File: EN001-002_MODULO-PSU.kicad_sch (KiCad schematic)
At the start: 90 parts, among them J1 2x5P 2.54mm, J2 Conn_01x02, J3 Barrel_Jack_Switch, J5 1x3P 2mm, J6 Conn_01x04, Q10 AO3401, Q11 KY6802, Q13 MMBT2222A, Q2 AO3401, Q3 KY6802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

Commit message: pcb layout
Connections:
- net GND: now also SW1.1 (A); no longer SW1.3 (C)
- net at R36.1: now also SW1.3 (C); no longer SW1.1 (A)
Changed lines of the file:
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@@
 		(lib_id "00_EV_DATABASE:SWITCH/SW_Slide_SPDT_Angled")
 		(at 31.75 147.32 0)
+		(mirror x)
 		(unit 1)
 		(exclude_from_sim no)
@@
 		(on_board yes)
 		(dnp no)
-		(fields_autoplaced yes)
 		(property "Reference" "SW1"
-			(at 31.75 138.43 0)
+			(at 31.75 156.21 0)
 			(effects
 				(font
@@
 		)
 		(property "Value" "SK12D07VG3"
-			(at 31.75 140.97 0)
+			(at 31.75 153.67 0)
 			(effects
 				(font
@@
 		)
 		(property "Datasheet" "~"
-			(at 31.75 154.94 0)
+			(at 31.75 139.7 0)
 			(effects
 				(font

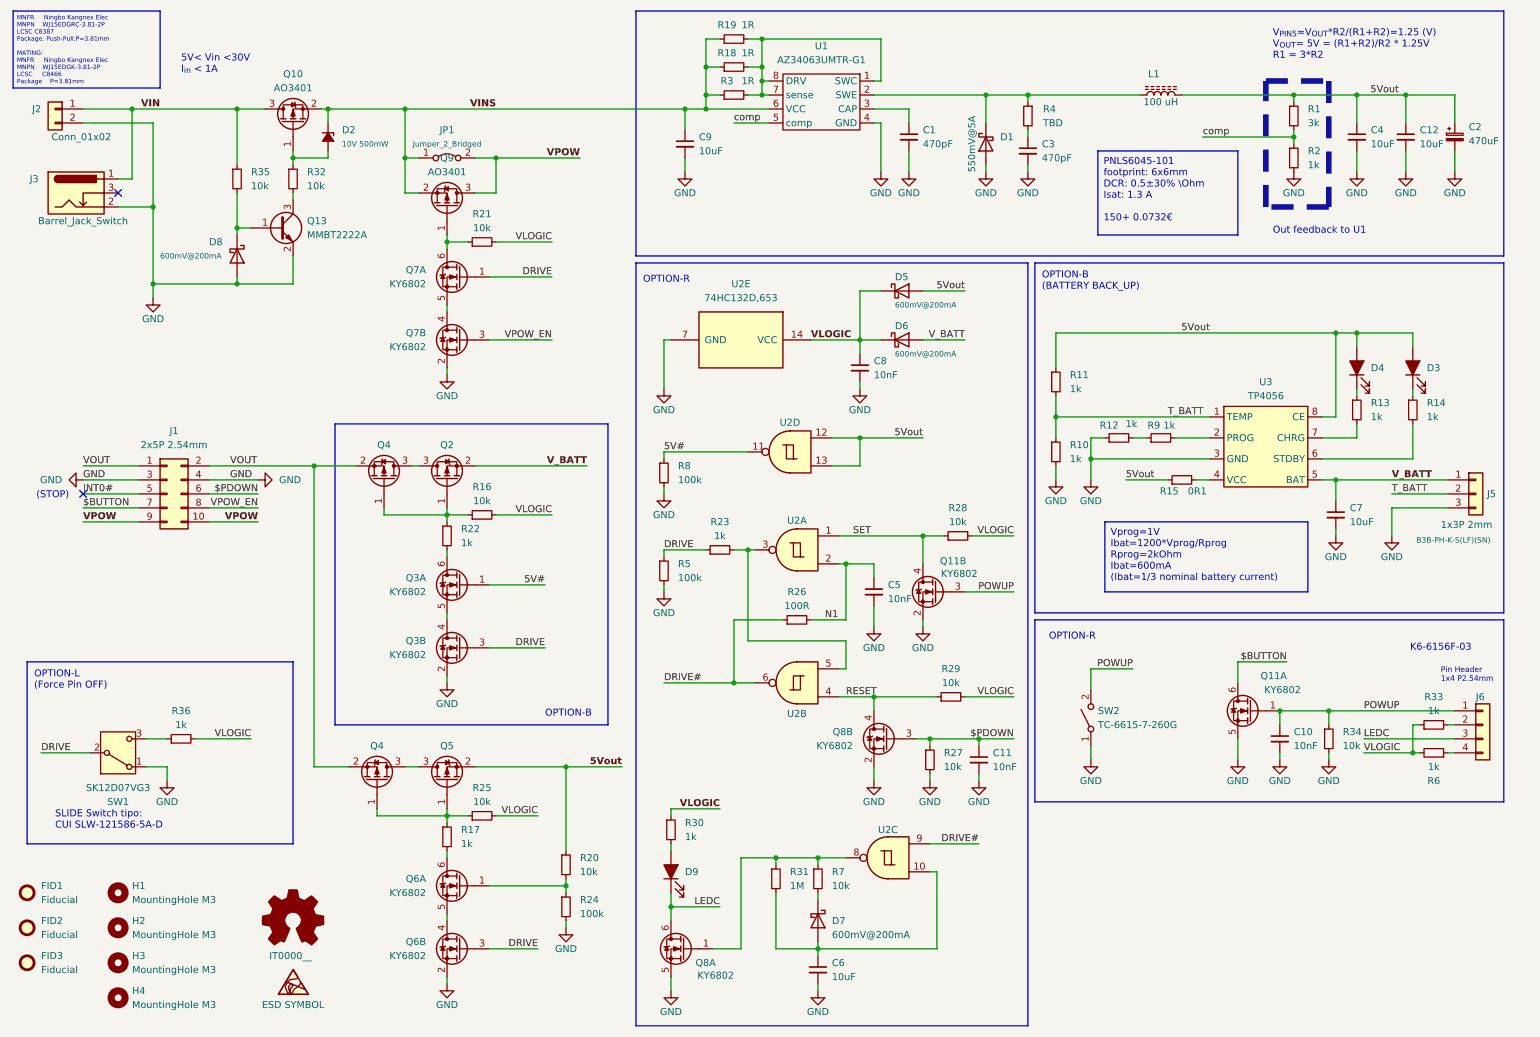
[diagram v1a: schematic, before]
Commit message: Rotated D7, SW2 in parallel to external switch, removed R26 replaced with short, removed C5
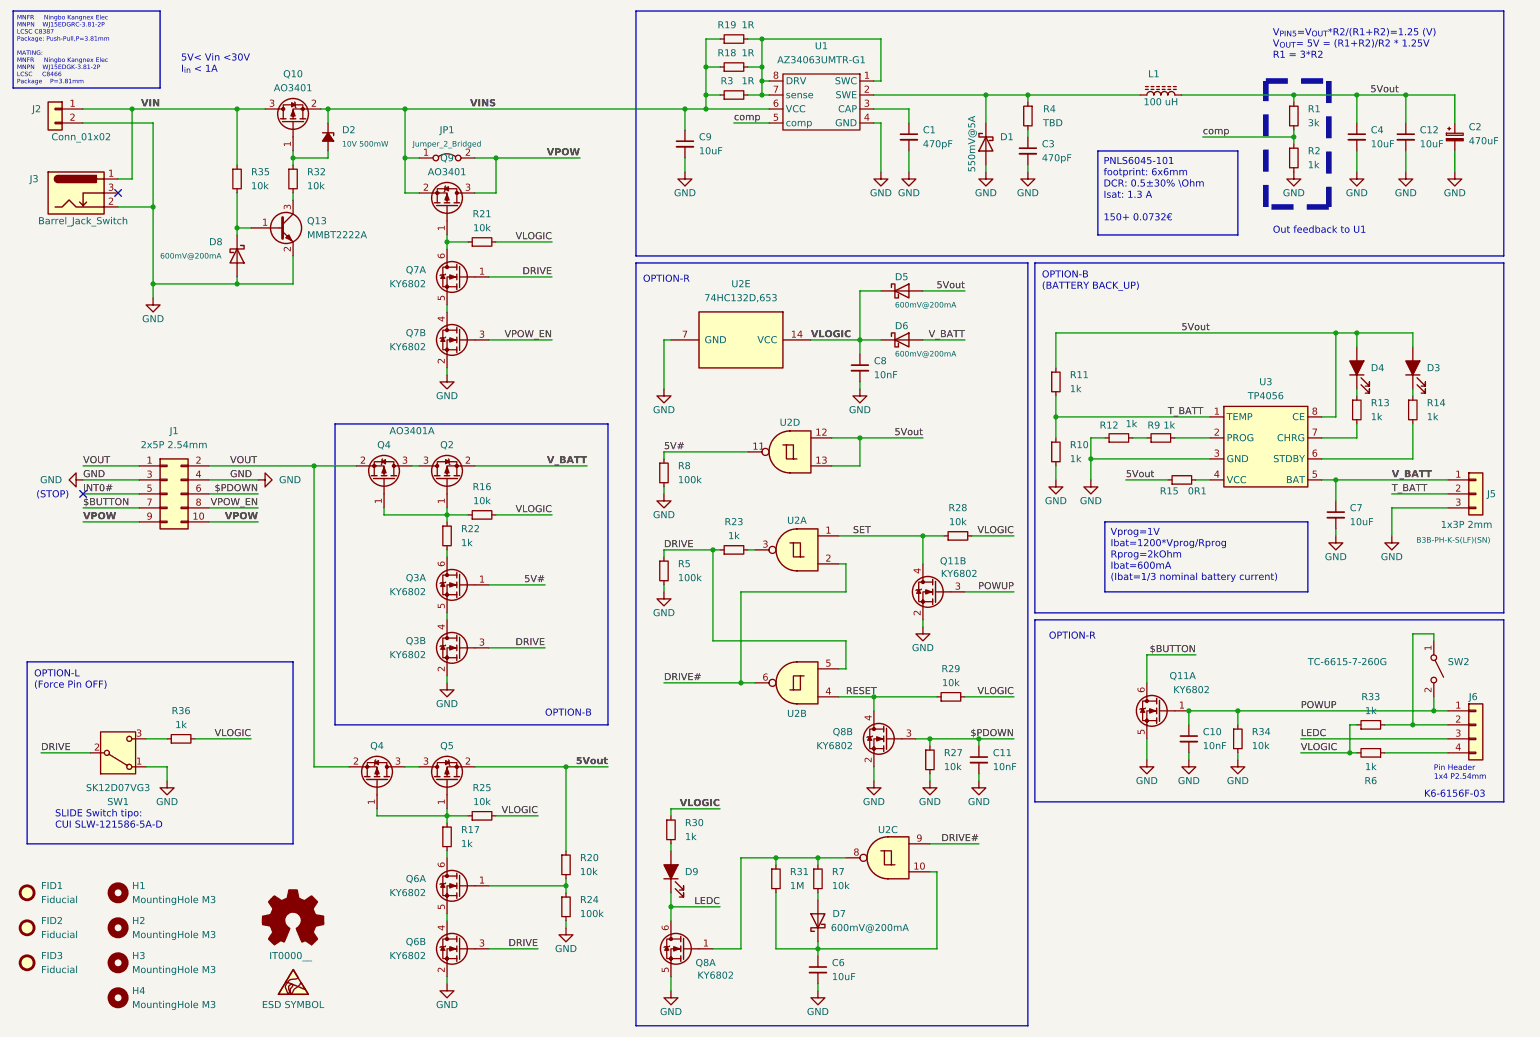
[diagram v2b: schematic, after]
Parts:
- removed C5: 10nF, Capacitor_SMD:C_0805_2012Metric_Pad1.18x1.45mm_HandSolder, symbol 00_EV_DATABASE:MLCC/CC0805KRX7R9BB103
- removed R26: 100R, Resistor_SMD:R_0805_2012Metric_Pad1.20x1.40mm_HandSolder, symbol 00_EV_DATABASE:Res-SMD/0805_100R
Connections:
- net N1 is gone; now on net DRIVE#: U2.2
- net DRIVE: now also U2.5
- net GND: no longer SW2.1 (A)
- net at J6.2 (Pin_2), R33.2: now also SW2.1 (A)
- net at R23.2, U2.3: no longer U2.5
- net at R7.2: now also D7.2 (A); no longer D7.1 (K)
- net at C6.1, R31.2, U2.10: now also D7.1 (K); no longer D7.2 (A)
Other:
- moved on the sheet: C10, D7, J6, Q11A, R23, R33, R34, R6, SW2

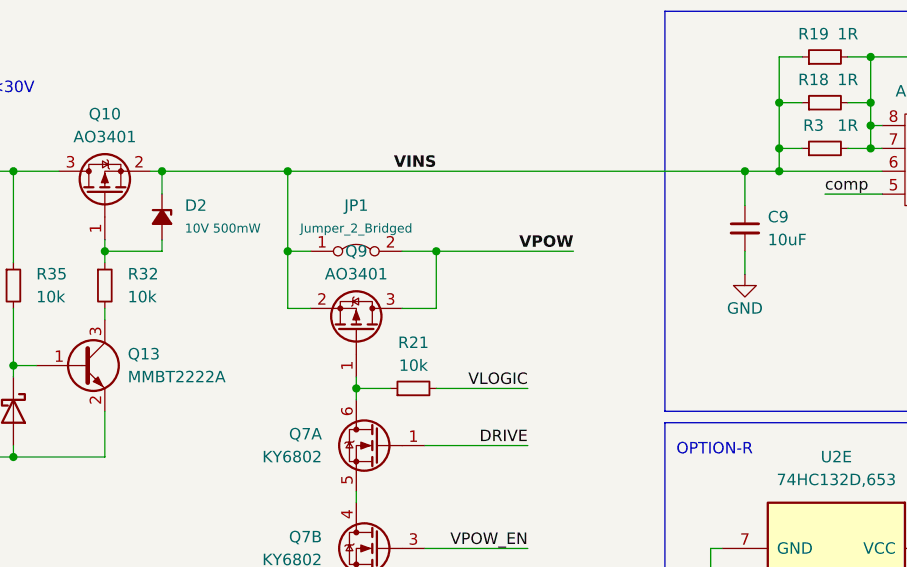
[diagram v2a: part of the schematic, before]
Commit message: R21 moved betwwen source and drain of Q9
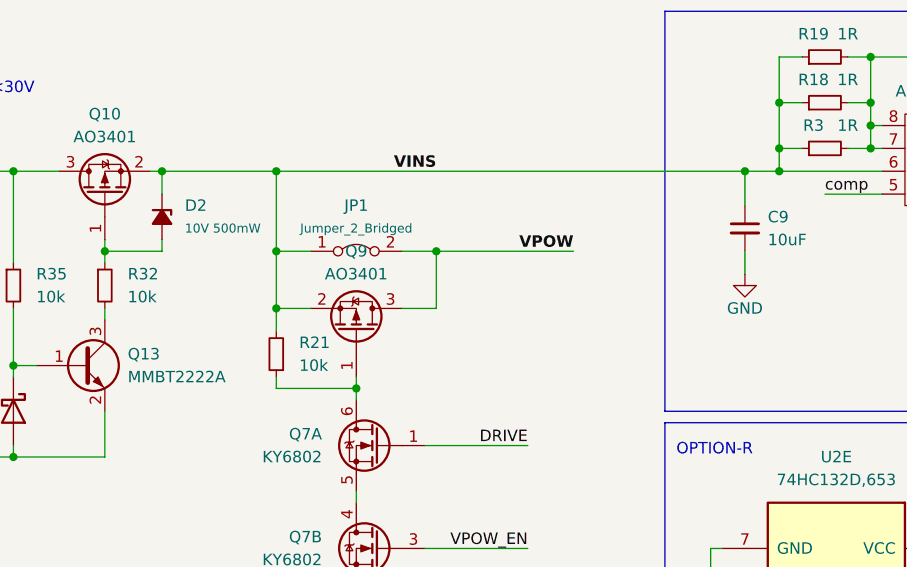
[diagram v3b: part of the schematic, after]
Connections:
- net VINS: now also R21.2
- net VLOGIC: no longer R21.2
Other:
- moved on the sheet: R21
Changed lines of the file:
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@@
 	)
 	(junction
+		(at 91.44 54.61)
+		(diameter 0)
+		(color 0 0 0 0)
+	)
+	(junction
 		(at 252.73 97.79)
 		(diameter 0)
@@
 	)
 	(junction
-		(at 113.03 149.86)
+		(at 82.55 30.48)
 		(diameter 0)
 		(color 0 0 0 0)
 	)
 	(junction
-		(at 91.44 54.61)
+		(at 113.03 149.86)
 		(diameter 0)
 		(color 0 0 0 0)
@@
 	)
 	(junction
-		(at 83.82 39.37)
-		(diameter 0)
-		(color 0 0 0 0)
-	)
-	(junction
 		(at 139.7 110.49)
 		(diameter 0)
@@
 	)
 	(junction
+		(at 82.55 45.72)
+		(diameter 0)
+		(color 0 0 0 0)
+	)
+	(junction
 		(at 166.37 90.17)
 		(diameter 0)
@@
 	)
 	(junction
+		(at 82.55 39.37)
+		(diameter 0)
+		(color 0 0 0 0)
+	)
+	(junction
 		(at 208.28 93.98)
 		(diameter 0)
@@
 	)
 	(junction
-		(at 83.82 30.48)
-		(diameter 0)
-		(color 0 0 0 0)
-	)
-	(junction
 		(at 113.03 171.45)
 		(diameter 0)
@@
 	(wire
 		(pts
-			(xy 91.44 55.88) (xy 91.44 54.61)
-		)
-		(stroke
-			(width 0)
-			(type default)
-		)
-	)
-	(wire
-		(pts
 			(xy 227.33 129.54) (xy 218.44 129.54)
 		)
@@
 	(wire
 		(pts
-			(xy 86.36 45.72) (xy 83.82 45.72)
-		)
-		(stroke
-			(width 0)
-			(type default)
-		)
-	)
-	(wire
-		(pts
 			(xy 189.23 27.94) (xy 168.91 27.94)
 		)
@@
 	(wire
 		(pts
-			(xy 83.82 30.48) (xy 83.82 39.37)
+			(xy 82.55 30.48) (xy 82.55 39.37)
 		)
 		(stroke
@@
 	(wire
 		(pts
+			(xy 82.55 54.61) (xy 91.44 54.61)
+		)
+		(stroke
+			(width 0)
+			(type default)
+		)
+	)
+	(wire
+		(pts
 			(xy 262.89 102.87) (xy 262.89 107.95)
 		)
@@
 	(wire
 		(pts
+			(xy 82.55 53.34) (xy 82.55 54.61)
+		)
+		(stroke
+			(width 0)
+			(type default)
+		)
+	)
+	(wire
+		(pts
 			(xy 163.83 113.03) (xy 163.83 118.11)
 		)
@@
 	(wire
 		(pts
-			(xy 162.56 132.08) (xy 163.83 132.08)
+			(xy 82.55 30.48) (xy 134.62 30.48)
 		)
 		(stroke
@@
 	(wire
 		(pts
-			(xy 132.08 157.48) (xy 132.08 158.75)
+			(xy 162.56 132.08) (xy 163.83 132.08)
 		)
 		(stroke
@@
 	(wire
 		(pts
-			(xy 100.33 54.61) (xy 110.49 54.61)
+			(xy 132.08 157.48) (xy 132.08 158.75)
 		)
 		(stroke
@@
 	(wire
 		(pts
-			(xy 83.82 39.37) (xy 86.36 39.37)
-		)
-		(stroke
-			(width 0)
-			(type default)
-		)
-	)
-	(wire
-		(pts
 			(xy 185.42 137.16) (xy 194.31 137.16)
 		)
@@
 	(wire
 		(pts
+			(xy 82.55 39.37) (xy 86.36 39.37)
+		)
+		(stroke
+			(width 0)
+			(type default)
+		)
+	)
+	(wire
+		(pts
 			(xy 256.54 27.94) (xy 265.43 27.94)
 		)
@@
 	(wire
 		(pts
+			(xy 82.55 48.26) (xy 82.55 45.72)
+		)
+		(stroke
+			(width 0)
+			(type default)
+		)
+	)
+	(wire
+		(pts
 			(xy 201.93 97.79) (xy 201.93 95.25)
 		)
@@
 	(wire
 		(pts
-			(xy 69.85 30.48) (xy 83.82 30.48)
+			(xy 69.85 30.48) (xy 82.55 30.48)
 		)
 		(stroke
@@
 	(wire
 		(pts
-			(xy 91.44 54.61) (xy 95.25 54.61)
+			(xy 40.64 149.86) (xy 36.83 149.86)
 		)
 		(stroke
@@
 	(wire
 		(pts
-			(xy 40.64 149.86) (xy 36.83 149.86)
+			(xy 270.51 125.73) (xy 266.7 125.73)
 		)
 		(stroke
@@
 	(wire
 		(pts
-			(xy 270.51 125.73) (xy 266.7 125.73)
+			(xy 91.44 53.34) (xy 91.44 54.61)
 		)
 		(stroke
@@
 	(wire
 		(pts
-			(xy 91.44 54.61) (xy 91.44 53.34)
+			(xy 218.44 129.54) (xy 218.44 134.62)
 		)
 		(stroke
@@
 	(wire
 		(pts
-			(xy 218.44 129.54) (xy 218.44 134.62)
+			(xy 166.37 63.5) (xy 166.37 72.39)
 		)
 		(stroke
@@
 	(wire
 		(pts
-			(xy 166.37 63.5) (xy 166.37 72.39)
+			(xy 158.75 173.99) (xy 158.75 172.72)
 		)
 		(stroke
@@
 	(wire
 		(pts
-			(xy 158.75 173.99) (xy 158.75 172.72)
+			(xy 82.55 45.72) (xy 86.36 45.72)
 		)
 		(stroke
@@
 	(wire
 		(pts
-			(xy 83.82 45.72) (xy 83.82 39.37)
+			(xy 82.55 45.72) (xy 82.55 39.37)
 		)
 		(stroke
@@
 	(wire
 		(pts
-			(xy 261.62 142.24) (xy 266.7 142.24)
+			(xy 91.44 54.61) (xy 91.44 55.88)
 		)
 		(stroke
@@
 	(wire
 		(pts
-			(xy 63.5 57.15) (xy 63.5 62.23)
+			(xy 261.62 142.24) (xy 266.7 142.24)
 		)
 		(stroke
@@
 	(wire
 		(pts
-			(xy 83.82 30.48) (xy 134.62 30.48)
+			(xy 63.5 57.15) (xy 63.5 62.23)
 		)
 		(stroke
@@
 	)
 	(label "VLOGIC"
-		(at 110.49 54.61 180)
-		(fields_autoplaced yes)
-		(effects
-			(font
-				(size 1.27 1.27)
-			)
-			(justify right bottom)
-		)
-	)
-	(label "VLOGIC"
 		(at 55.88 144.78 180)
 		(fields_autoplaced yes)
@@
 	(symbol
 		(lib_id "00_EV_DATABASE:Res-SMD/0805_10k")
-		(at 97.79 54.61 90)
+		(at 82.55 50.8 180)
 		(unit 1)
 		(exclude_from_sim no)
@@
 		(fields_autoplaced yes)
 		(property "Reference" "R21"
-			(at 97.79 49.53 90)
+			(at 85.09 49.5299 0)
 			(effects
 				(font
 					(size 1.27 1.27)
 				)
+				(justify right)
 			)
 		)
 		(property "Value" "10k"
-			(at 97.79 52.07 90)
+			(at 85.09 52.0699 0)
 			(effects
 				(font
 					(size 1.27 1.27)
 				)
+				(justify right)
 			)
 		)
 		(property "Footprint" "Resistor_SMD:R_0805_2012Metric_Pad1.20x1.40mm_HandSolder"
-			(at 97.79 54.61 0)
+			(at 82.55 50.8 0)
 			(effects
 				(font
@@
 		)
 		(property "Datasheet" "~"
-			(at 97.79 54.61 0)
+			(at 82.55 50.8 0)
 			(effects
 				(font
@@
 		)
 		(property "Description" "Thin Film Resistor 10kΩ 125mW 150V ±1% ±100ppm/℃ "
-			(at 97.79 54.61 0)
+			(at 82.55 50.8 0)
 			(effects
 				(font
@@
 		)
 		(property "MNFR-1" "UNI-ROYAL"
-			(at 97.79 54.61 0)
+			(at 82.55 50.8 0)
 			(show_name yes)
 			(effects
@@
 		)
 		(property "MNFR-1-PN" "0805W8F1002T5E"
-			(at 97.79 54.61 0)
+			(at 82.55 50.8 0)
 			(show_name yes)
 			(effects
@@
 		)
 		(property "SUPP-1" "LCSC"
-			(at 97.79 54.61 0)
+			(at 82.55 50.8 0)
 			(show_name yes)
 			(effects
@@
 		)
 		(property "SUPP-1-CODE" "C17414"
-			(at 97.79 54.61 0)
+			(at 82.55 50.8 0)
 			(show_name yes)
 			(effects
@@
 		)
 		(property "Case" "0805"
-			(at 97.79 54.61 0)
+			(at 82.55 50.8 0)
 			(show_name yes)
 			(effects
@@
 		)
 		(property "STOCK" "1000"
-			(at 97.79 54.61 0)
+			(at 82.55 50.8 0)
 			(show_name yes)
 			(effects
@@
 		)
 		(property "SUPP-1-UNIT-PRICE" "0.0013"
-			(at 97.79 54.61 0)
+			(at 82.55 50.8 0)
 			(effects
 				(font

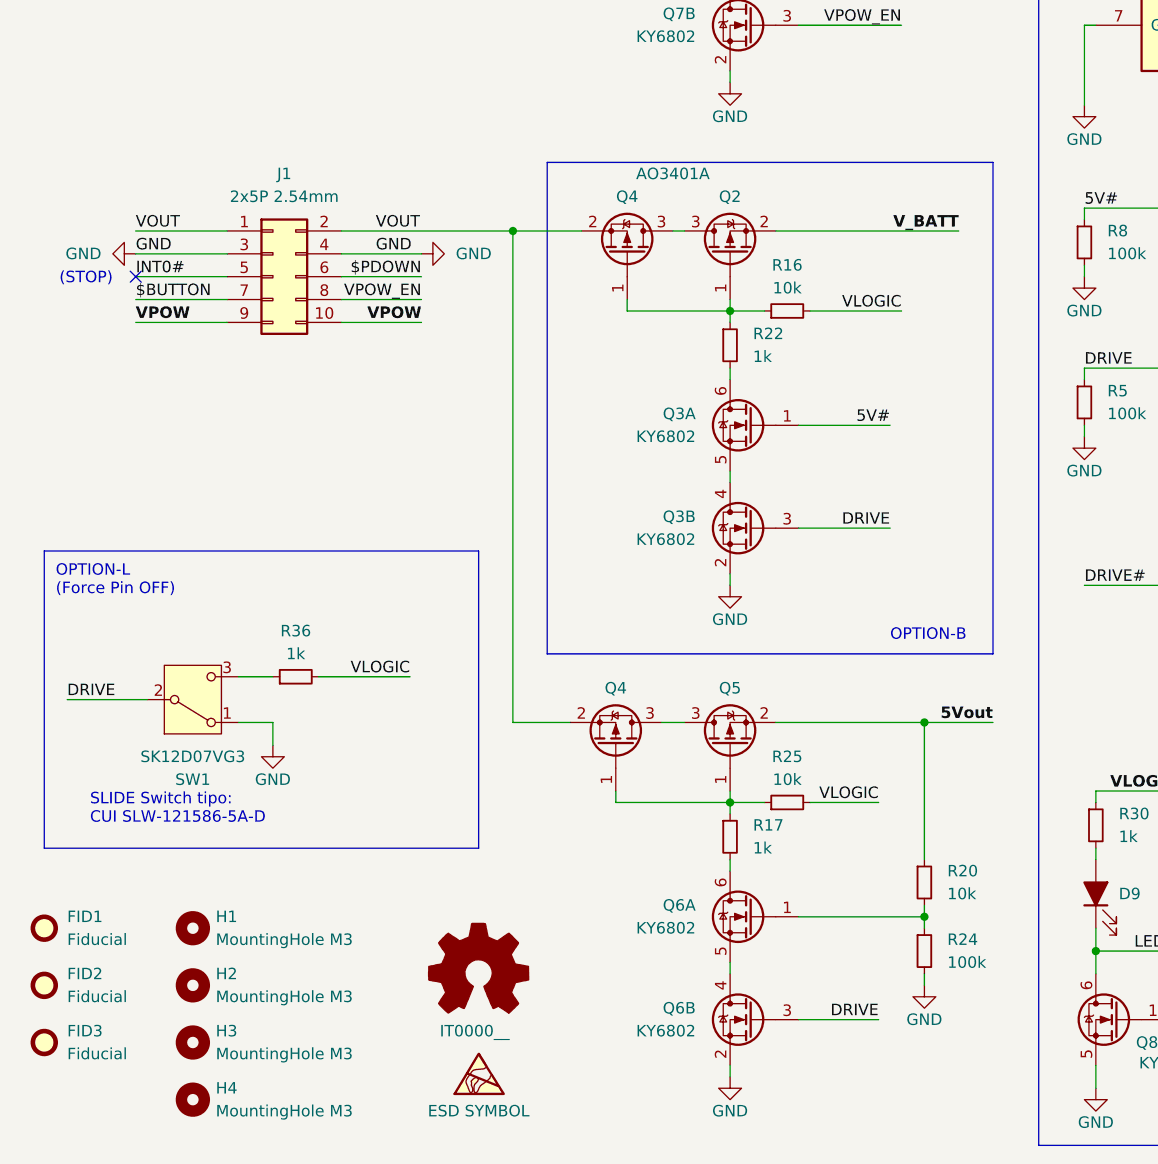
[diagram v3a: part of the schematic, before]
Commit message: Added R26 and R37 100k pulldown on back-to-back pass mosfet
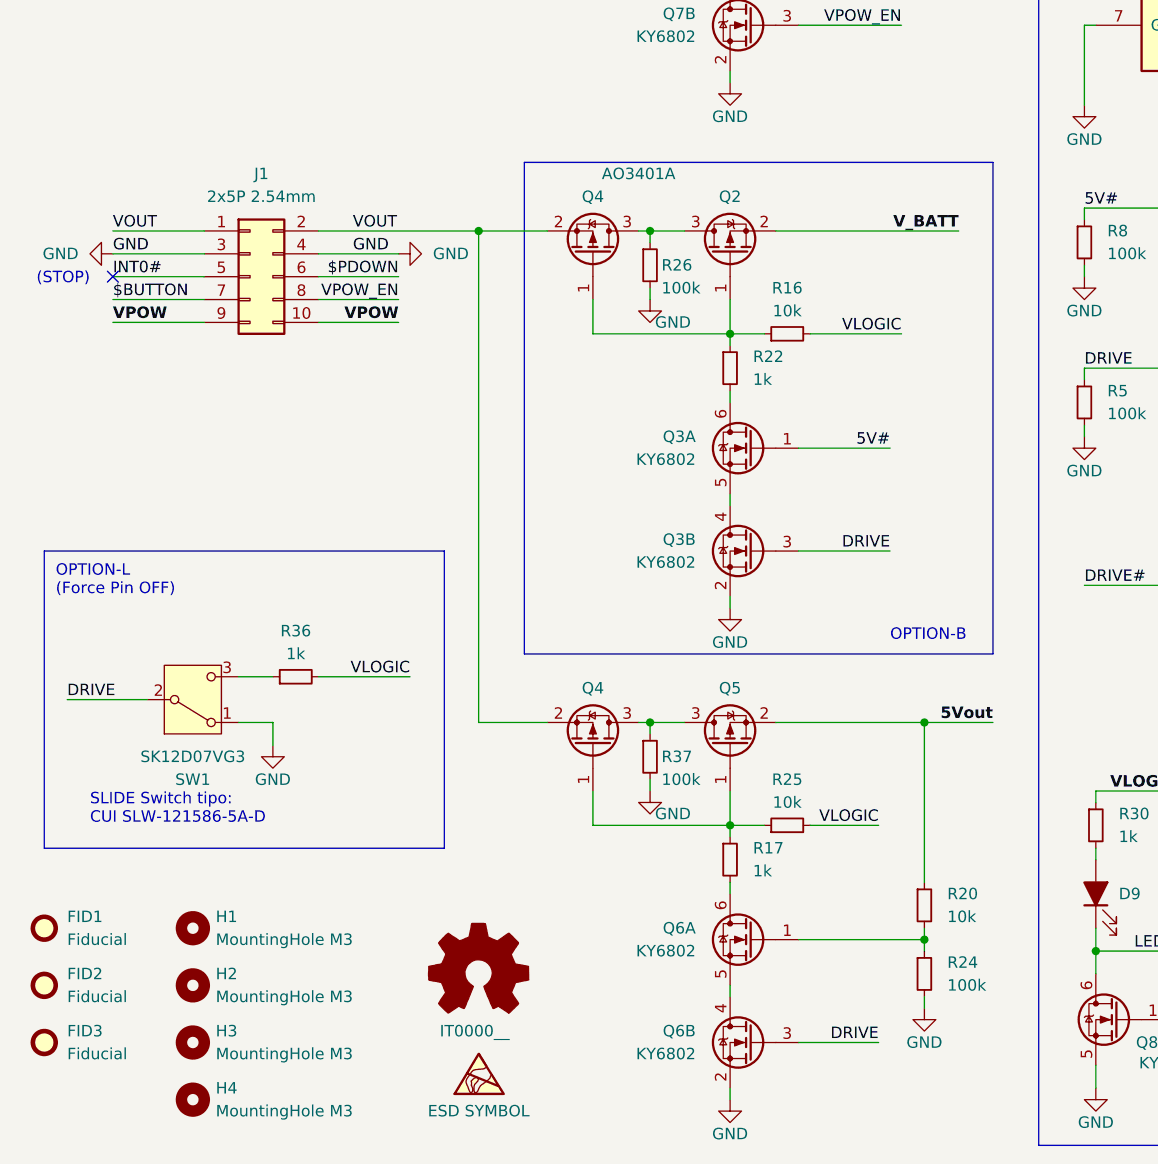
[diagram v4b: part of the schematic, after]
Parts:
- added R26, R37: 100k, Resistor_SMD:R_0805_2012Metric_Pad1.20x1.40mm_HandSolder, symbol 00_EV_DATABASE:Res-SMD/0805_100k
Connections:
- net GND: now also R26.2, R37.2
- net at Q4.3 (D), Q5.3 (D): now also R37.1
- net at Q2.3 (D), Q4.3 (D): now also R26.1
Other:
- moved on the sheet: J1, Q3A, Q3B, Q4, Q6A, Q6B, R16, R17, R20, R22, R24, R25
